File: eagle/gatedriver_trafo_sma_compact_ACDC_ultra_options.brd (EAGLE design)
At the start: 101.9 x 165.1 mm, 98 parts, among them K1 G5V-2, X4 BU-SMA-V

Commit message: gd mods
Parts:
- added U$23, U$24, U$25, U$30: VP2450, transistor-fet:SOT89-BCE
- added U$26, U$27, U$28, U$29: VN2450, transistor-fet:SOT89-BCE
- moved C3 17.8 mm to (116.1, 102.1)
- moved HV1 17.8 mm to (105.4, 159.3)
- moved HV2 17.8 mm to (105.7, 7.87)
- moved OUT 17.8 mm to (116.1, 81.3)
- moved R10 17.8 mm to (104.6, 35.1)
- moved R11 17.8 mm to (104.6, 17.3)
- moved R15 17.8 mm to (101.9, 110.2)
- moved R16 17.8 mm to (101.9, 90.7)
- moved R22 17.8 mm to (101.9, 67.6)
- moved R23 17.8 mm to (104.6, 50.3)
- moved R33 17.8 mm to (97.8, 121.2)
- moved R35 17.8 mm to (115.8, 70.9)
- moved R36 17.8 mm to (115.8, 57.9)
- moved R37 17.8 mm to (116.1, 93.0)
- moved R4 17.8 mm to (102.1, 146.1)
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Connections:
- net N$11: now also U$29.B
- net N$12: now also U$25.B
- net N$13: now also U$29.C, U$29.C@1
- net N$18: now also U$25.C, U$25.C@1
- net N$19: now also U$26.E
- net N$20: now also U$25.E
- net N$21: now also U$24.E
- net N$251: now also U$28.B
- net N$26: now also U$26.C, U$26.C@1, U$30.C, U$30.C@1
- net N$3: now also U$29.E
- net N$31: now also U$30.E
- net N$32: now also U$24.C, U$24.C@1
- net N$33: now also U$23.C, U$23.C@1
- net N$34: now also U$30.B
- net N$36: now also U$23.B
- net N$39: now also U$23.E
- net N$46: now also U$27.C, U$27.C@1
- net N$47: now also U$27.B
- net N$50: now also U$26.B
- net N$51: now also U$28.C, U$28.C@1
- net N$6: now also U$28.E
- net N$8: now also U$24.B
- net N$9: now also U$27.E
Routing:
- net N$32: track 87.9 -> 144.7 mm
- net N$26: track 61.7 -> 103.7 mm
- net N$33: track 80.4 -> 121.2 mm
- net N$18: track 100.9 -> 139.0 mm
- net GND: track 390.2 -> 427.5 mm
- net N$13: track 68.6 -> 105.5 mm
- net N$46: track 64.9 -> 101.1 mm
- net N$17: track 76.5 -> 111.0 mm
- net N$31: track 3.08 -> 32.1 mm, vias 0 -> 1
- net N$51: track 84.5 -> 112.2 mm
- net N$3: track 3.05 -> 28.9 mm
- net N$9: track 4.45 -> 27.5 mm
- net N$19: track 4.09 -> 25.6 mm
- net N$21: track 3.29 -> 24.0 mm
- net N$47: track 19.1 -> 39.2 mm
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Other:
- board size 101.9 x 165.1 mm -> 119.6 x 165.1 mm

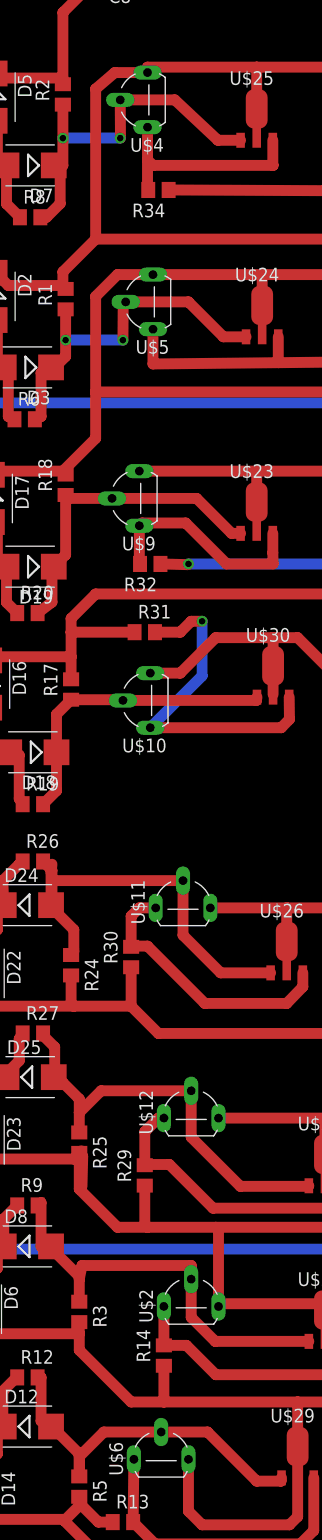
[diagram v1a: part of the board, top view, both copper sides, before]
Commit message: Square wave one side/dc other
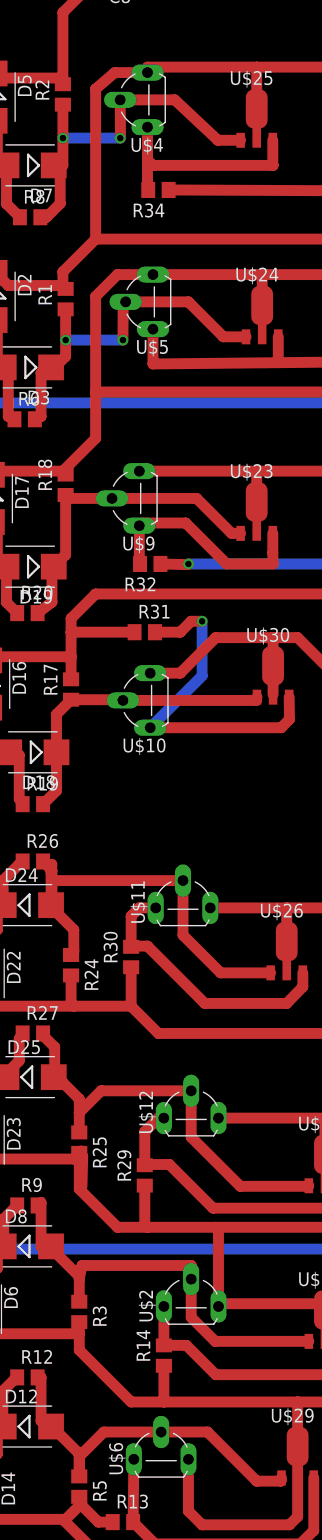
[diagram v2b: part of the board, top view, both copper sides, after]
